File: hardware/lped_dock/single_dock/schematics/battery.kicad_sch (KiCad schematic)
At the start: 9 parts, among them IC1 BQ24050DSQR

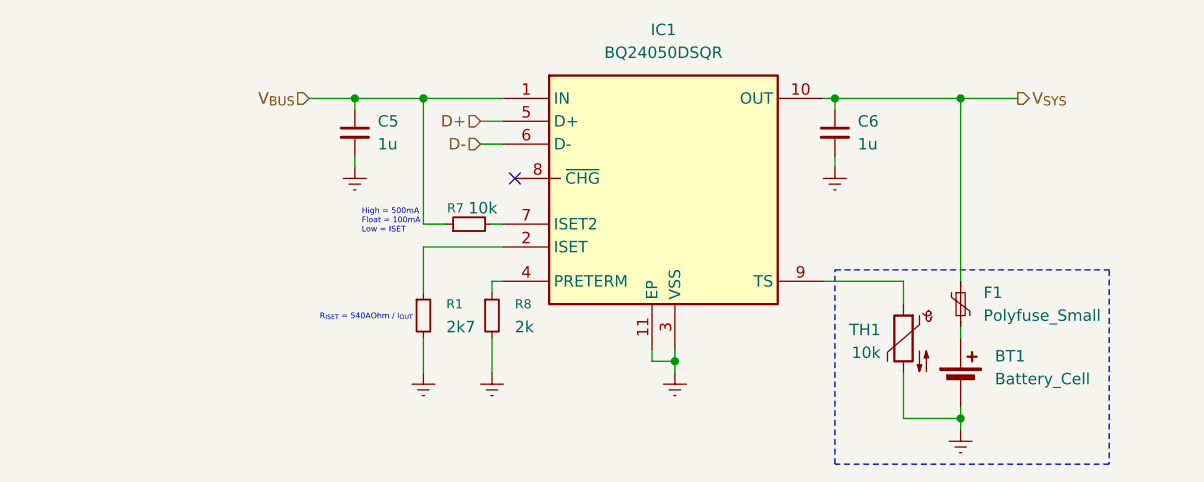
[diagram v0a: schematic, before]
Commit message: feat(hardware): improvements to dock battery system
* Added current limiting resistor to battery
* Added charging status LED
* Changed side of battery connector
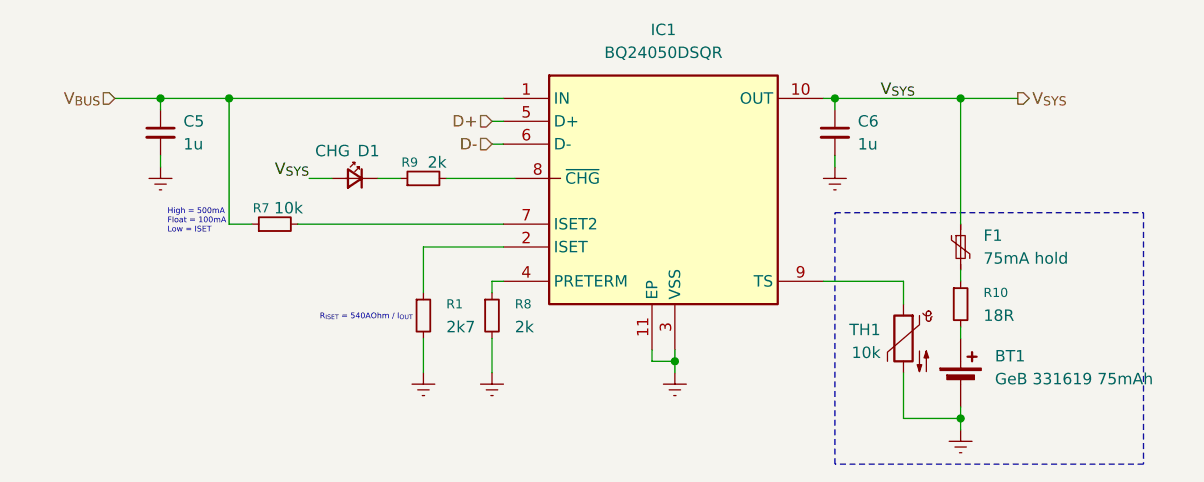
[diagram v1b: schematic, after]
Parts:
- added D1: CHG, LED_SMD:LED_0805_2012Metric, symbol Device:LED_Small
- added R10: 18R, Resistor_SMD:R_0603_1608Metric, symbol Device:R_Small
- added R9: 2k, Resistor_SMD:R_0402_1005Metric, symbol Device:R_Small
- BT1: value Battery_Cell -> GeB 331619 75mAh
- F1: value Polyfuse_Small -> 75mA hold
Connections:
- net V_{SYS}: now also D1.2 (A)
- net at F1.2: now also R10.1; no longer BT1.1 (+)
- net at IC1.8 (~{CHG}): now also R9.2
- new net: BT1.1 (+), R10.2
- new net: D1.1 (K), R9.1
- no-connect marks 1 -> 0
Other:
- moved on the sheet: C5, F1, R7

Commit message: fix(hardware): minor fixes before manufacturing
Changed footprint of USB protection diode
Changed footprint of Programmer fuse
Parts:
- R10: footprint Resistor_SMD:R_0603_1608Metric -> Resistor_SMD:R_1206_3216Metric
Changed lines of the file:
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@@
 			)
 		)
-		(property "Footprint" "Resistor_SMD:R_0603_1608Metric"
+		(property "Footprint" "Resistor_SMD:R_1206_3216Metric"
 			(at 161.29 90.17 0)
 			(effects
